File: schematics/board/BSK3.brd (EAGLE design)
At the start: 82 x 100 mm, 27 parts

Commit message: Подписаны разъемы на платах
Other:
- board text added: "to BSK1"
- board text added: "to BSK5"
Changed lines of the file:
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@@
 <text x="53.3" y="9.1" size="1.778" layer="26" rot="MR0">BSK3 "Концерн ИТС"</text>
 <circle x="41" y="50" radius="15.25" width="0.2" layer="20"/>
+<text x="35.3" y="95.1" size="1.778" layer="26" rot="MR0">to BSK1</text>
+<text x="41.1" y="2.8" size="1.778" layer="26" rot="MR0">to BSK5</text>
 </plain>
 <attributes>

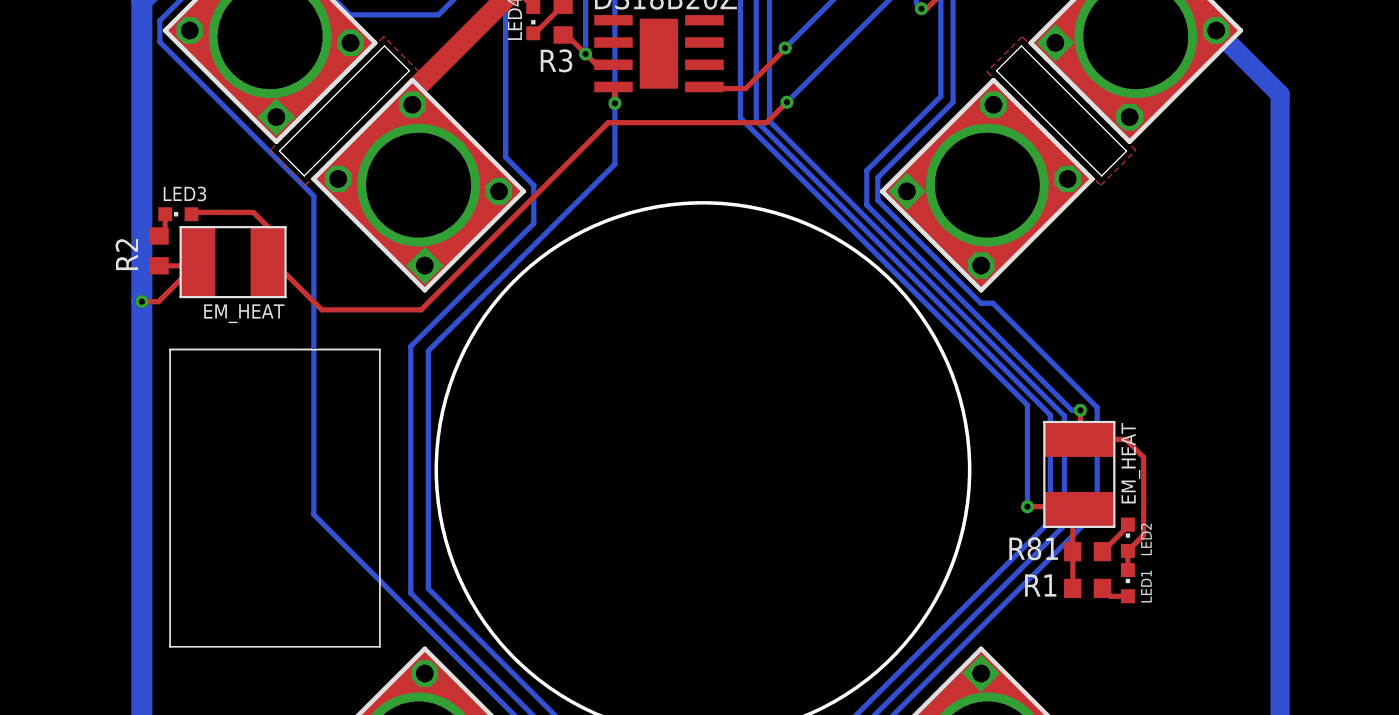
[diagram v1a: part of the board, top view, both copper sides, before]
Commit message: Внесены косметические изменения на БСК2 и БСК3
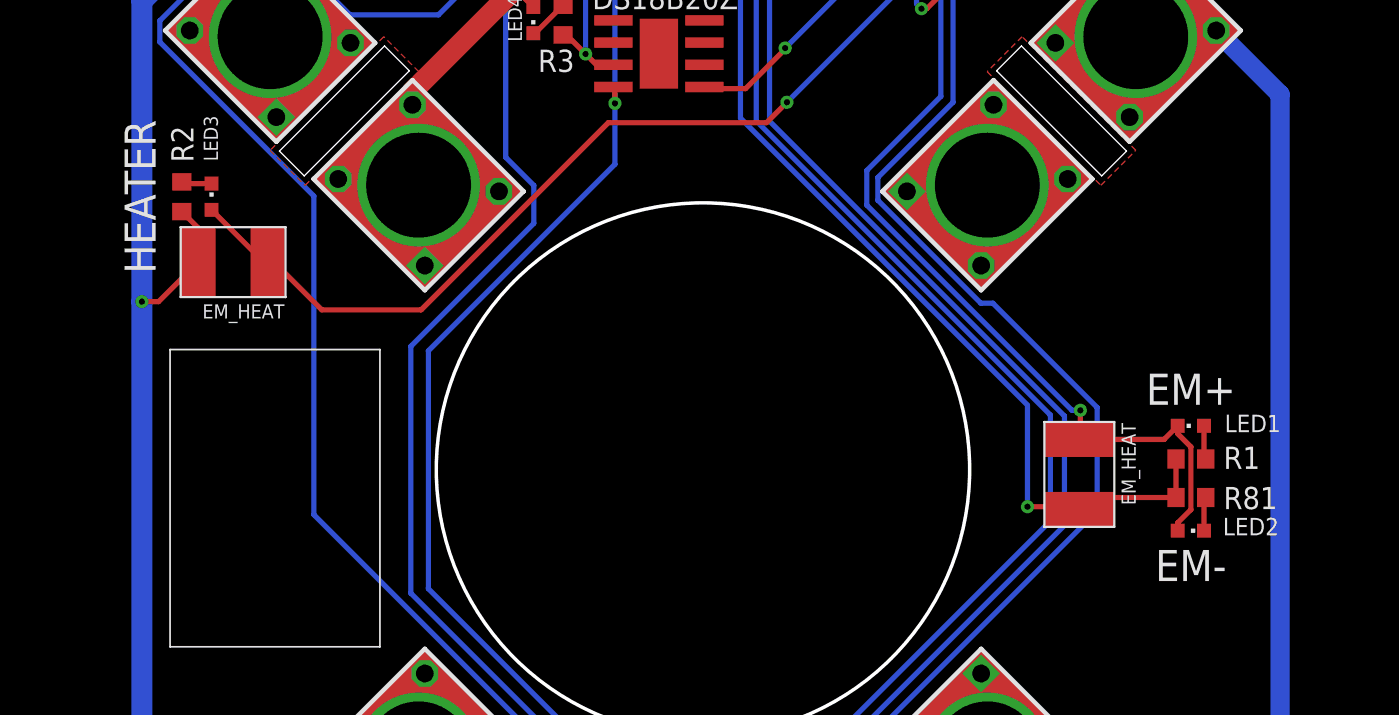
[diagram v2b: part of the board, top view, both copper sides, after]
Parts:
- moved LED1 9.69 mm to (68.9, 52.5), turned to 90 degrees
- moved R1 9.46 mm to (68.9, 50.6)
- moved R81 6.66 mm to (68.9, 48.4)
- moved LED2 3.62 mm to (68.9, 46.5), turned to 270 degrees
- moved R2 3.36 mm to (11.2, 65.6)
- moved LED3 2.15 mm to (12.9, 65.6), turned to 0 degrees
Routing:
- net N$2: track 61.0 -> 64.8 mm
- net N$3: track 55.3 -> 53.0 mm
- net N$1: track 59.2 -> 60.9 mm
- net GND: track 201.8 -> 202.7 mm
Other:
- board text added: "EM+"
- board text added: "EM-"
- board text added: "HEATER"

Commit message: Платы подготовлены для Резонита
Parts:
- removed U$14: FS8205A, CanCubeSat:FS8205A
- added FS8205A: FS8205A+, CanCubeSat:FS8205A+
- renumbered U$5 to DS18B20Z, U$8 to L293DD
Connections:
- net BUS-: now also FS8205A.23; no longer U$14.23
- net GND: now also FS8205A.67; no longer U$14.67
- net HEAT: now also FS8205A.HEAT; no longer U$14.HEAT
- net N$8: now also FS8205A.4; no longer U$14.4
- net N$9: now also FS8205A.5; no longer U$14.5
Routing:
- net N$2: track 64.8 -> 64.3 mm
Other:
- board text added: "BUS"

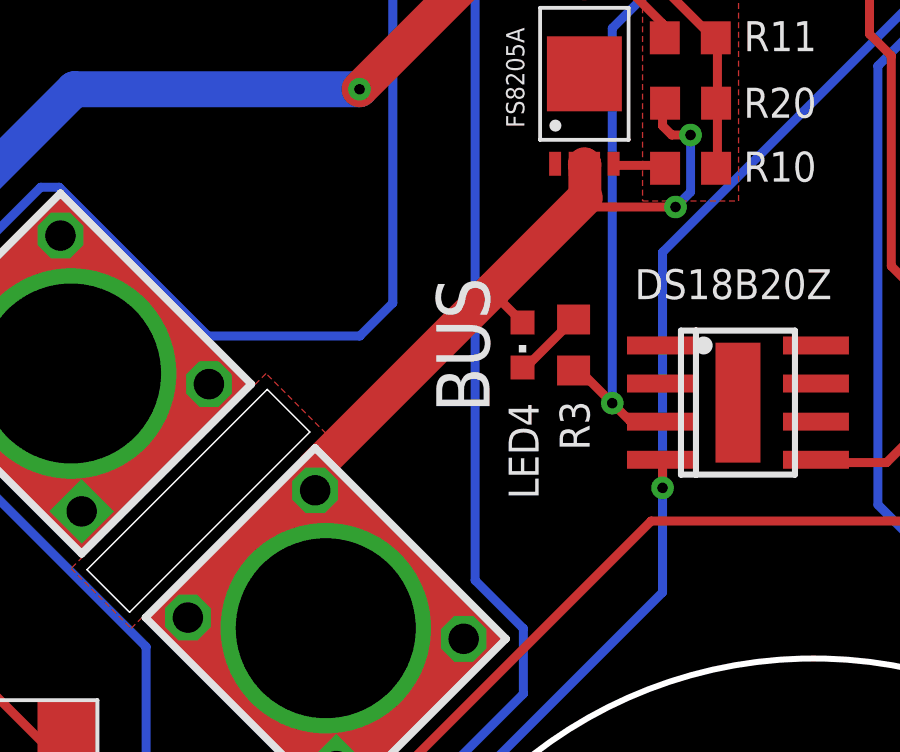
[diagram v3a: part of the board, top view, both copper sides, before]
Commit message: Исправлены RADIO и диоды
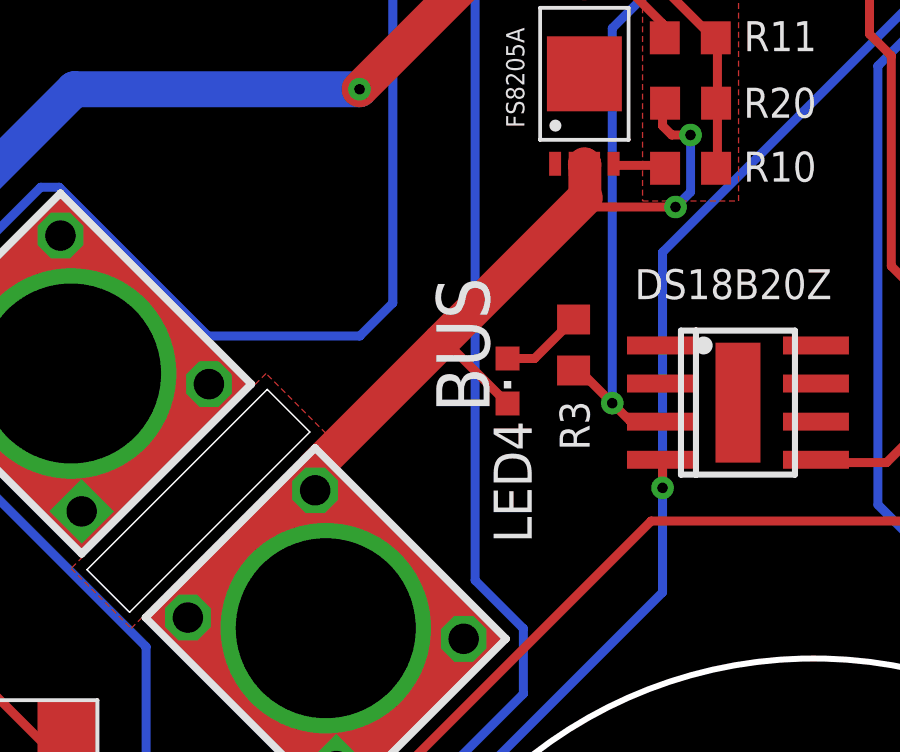
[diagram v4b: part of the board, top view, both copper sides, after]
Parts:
- moved LED4 1.30 mm to (30.8, 74.5)
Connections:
- net BUS-: now also LED4.C; no longer LED4.A
- net N$7: now also LED4.A; no longer LED4.C
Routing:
- net BUS-: track 42.9 -> 44.5 mm
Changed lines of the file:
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@@
 <attribute name="VALUE" x="14.805" y="64.33" size="1.27" layer="27" rot="R90"/>
-</element>
-<element name="LED4" library="led" library_urn="urn:adsk.eagle:library:259" package="CHIPLED_0603" package3d_urn="urn:adsk.eagle:package:15822/2" value="" x="31.3" y="75.7" smashed="yes" rot="R180">
-<attribute name="NAME" x="30.835" y="73.77" size="1" layer="25" rot="R270"/>
-<attribute name="POPULARITY" value="28" x="50.9" y="79.4" size="1.778" layer="27" rot="R180" display="off"/>
-<attribute name="VALUE" x="29.395" y="76.97" size="1.27" layer="27" rot="R270"/>
 </element>
 <element name="R3" library="resistor" library_urn="urn:adsk.eagle:library:348" package="R0603" package3d_urn="urn:adsk.eagle:package:23555/3" value="2k" x="33" y="75.7" smashed="yes" rot="R90">
 <attribute name="NAME" x="32.535" y="73.835" size="1" layer="25" rot="R270"/>
 <attribute name="VALUE" x="34.905" y="75.065" size="1.27" layer="27" rot="R90"/>
+</element>
+<element name="LED4" library="led" library_urn="urn:adsk.eagle:library:259" package="CHIPLED_0603" package3d_urn="urn:adsk.eagle:package:15822/2" value="" x="30.8" y="74.5" smashed="yes" rot="R180">
+<attribute name="NAME" x="30.335" y="73.17" size="1.27" layer="25" rot="R270"/>
+<attribute name="POPULARITY" value="28" x="35.7" y="68.9" size="1.778" layer="27" rot="R180" display="off"/>
+<attribute name="VALUE" x="28.895" y="75.77" size="1.27" layer="27" rot="R270"/>
 </element>
 </elements>
@@
 <wire x1="29.2608" y1="65.8368" x2="29.33619375" y2="65.90644375" width="0.3" layer="1"/>
 <wire x1="24.9936" y1="65.8368" x2="24.74" y2="66.26" width="0.3" layer="1"/>
-<contactref element="LED4" pad="A"/>
-<wire x1="33.3756" y1="80.6" x2="30.2878" y2="77.5122" width="1.2" layer="1"/>
-<wire x1="31.3" y1="76.45" x2="30.2878" y2="77.4622" width="0.3" layer="1"/>
-<wire x1="30.2878" y1="77.4622" x2="30.2878" y2="77.5122" width="0.3" layer="1"/>
+<wire x1="33.3756" y1="80.6" x2="28.5878" y2="75.8122" width="1.2" layer="1"/>
 <wire x1="35.9664" y1="83.0056" x2="36.272" y2="82.7" width="0.3" layer="1"/>
 <wire x1="36.272" y1="82.7" x2="36.9" y2="82.7" width="0.3" layer="1"/>
@@
 <wire x1="24.74" y1="66.26" x2="24.74" y2="70.5026375" width="0.3" layer="1"/>
 <wire x1="24.74" y1="70.5026375" x2="24.38644375" y2="70.85619375" width="0.3" layer="1"/>
-<wire x1="30.2878" y1="77.5122" x2="24.38644375" y2="71.61084375" width="1.2" layer="1"/>
+<wire x1="28.5878" y1="75.8122" x2="24.38644375" y2="71.61084375" width="1.2" layer="1"/>
 <wire x1="24.38644375" y1="71.61084375" x2="24.38644375" y2="70.85619375" width="1.2" layer="1"/>
+<contactref element="LED4" pad="C"/>
+<wire x1="28.5878" y1="75.8122" x2="28.7378" y2="75.8122" width="0.3" layer="1"/>
+<wire x1="28.7378" y1="75.8122" x2="30.8" y2="73.75" width="0.3" layer="1"/>
 </signal>
 <signal name="N$8">
@@
 </signal>
 <signal name="N$7">
+<contactref element="LED4" pad="A"/>
 <contactref element="R3" pad="2"/>
-<contactref element="LED4" pad="C"/>
-<wire x1="33" y1="76.55" x2="31.4" y2="74.95" width="0.3" layer="1"/>
-<wire x1="31.4" y1="74.95" x2="31.3" y2="74.95" width="0.3" layer="1"/>
+<wire x1="33" y1="76.55" x2="31.7" y2="75.25" width="0.3" layer="1"/>
+<wire x1="31.7" y1="75.25" x2="30.8" y2="75.25" width="0.3" layer="1"/>
 </signal>
 </signals>

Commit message: Резисторы у FS8205A 100Ом
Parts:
- R10, R11: value 10k -> 100R
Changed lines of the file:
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@@
 </autorouter>
 <elements>
-<element name="R10" library="resistor" library_urn="urn:adsk.eagle:library:348" package="R0603" package3d_urn="urn:adsk.eagle:package:23555/3" value="10k" x="36.9" y="81.59" smashed="yes" rot="R180">
+<element name="R10" library="resistor" library_urn="urn:adsk.eagle:library:348" package="R0603" package3d_urn="urn:adsk.eagle:package:23555/3" value="100R" x="36.9" y="81.59" smashed="yes" rot="R180">
 <attribute name="NAME" x="38.665" y="81.145" size="1" layer="25"/>
 <attribute name="VALUE" x="37.535" y="83.495" size="1.27" layer="27" rot="R180"/>
 </element>
-<element name="R11" library="resistor" library_urn="urn:adsk.eagle:library:348" package="R0603" package3d_urn="urn:adsk.eagle:package:23555/3" value="10k" x="36.89" y="85.94" smashed="yes" rot="R180">
+<element name="R11" library="resistor" library_urn="urn:adsk.eagle:library:348" package="R0603" package3d_urn="urn:adsk.eagle:package:23555/3" value="100R" x="36.89" y="85.94" smashed="yes" rot="R180">
 <attribute name="NAME" x="38.675" y="85.495" size="1" layer="25"/>
 <attribute name="VALUE" x="37.525" y="87.845" size="1.27" layer="27" rot="R180"/>

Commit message: Добавлены новые диоды
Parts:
- added LAP4: LAP4-BOTTOM, led:P47F-BOTTOM
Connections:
- net BUS-: now also LAP4.C
- net N$7: now also LAP4.A
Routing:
- net BUS-: track 44.5 -> 104.9 mm, vias 2 -> 5
- net N$7: track 2.74 -> 61.5 mm, vias 0 -> 4
- net B5_KEM-: track 128.0 -> 135.1 mm
- net GND: track 202.7 -> 206.4 mm
